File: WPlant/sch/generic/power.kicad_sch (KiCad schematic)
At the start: 47 parts, among them J2 Battery, J3 Balance, J4 DE9_Receptacle, J5 220V, U2 AP64352SP-13, U3 AP64352SP-13, U4 AP64352SP-13, U6 AP2204R-5.0

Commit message: Almost finished WP Generic
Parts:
- C10, C11, C12, C17, C18, C19, C23, C24, C25, C28, C29: footprint (none) -> Capacitor_SMD:C_0603_1608Metric_Pad1.08x0.95mm_HandSolder
- C13, C14, C15, C16, C20, C21, C22, C26, C43: footprint (none) -> Capacitor_SMD:C_1206_3216Metric_Pad1.33x1.80mm_HandSolder
- J2: footprint (none) -> local:pins4x10
- J3: footprint (none) -> Connector_JST:JST_XH_B5B-XH-A_1x05_P2.50mm_Vertical
- J4: footprint (none) -> easyeda2kicad:DB9-TH_LD09P33E4GV00LF
- R10, R11, R12, R13, R14, R15, R16, R17, R18, R20: footprint (none) -> Resistor_SMD:R_0603_1608Metric_Pad0.98x0.95mm_HandSolder
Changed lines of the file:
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@@
 			)
 		)
-		(property "Footprint" ""
+		(property "Footprint" "Capacitor_SMD:C_0603_1608Metric_Pad1.08x0.95mm_HandSolder"
 			(at 73.66 133.6548 0)
 			(effects
@@
 			)
 		)
-		(property "Footprint" ""
+		(property "Footprint" "Capacitor_SMD:C_0603_1608Metric_Pad1.08x0.95mm_HandSolder"
 			(at 86.6648 53.34 0)
 			(effects
@@
 			)
 		)
-		(property "Footprint" ""
+		(property "Footprint" "Resistor_SMD:R_0603_1608Metric_Pad0.98x0.95mm_HandSolder"
 			(at 49.022 167.64 90)
 			(effects
@@
 			)
 		)
-		(property "Footprint" ""
+		(property "Footprint" "easyeda2kicad:DB9-TH_LD09P33E4GV00LF"
 			(at 214.63 43.18 0)
 			(effects
@@
 			)
 		)
-		(property "Footprint" ""
+		(property "Footprint" "Capacitor_SMD:C_1206_3216Metric_Pad1.33x1.80mm_HandSolder"
 			(at 141.2748 104.14 0)
 			(effects
@@
 			)
 		)
-		(property "Footprint" ""
+		(property "Footprint" "Capacitor_SMD:C_0603_1608Metric_Pad1.08x0.95mm_HandSolder"
 			(at 117.1448 99.06 0)
 			(effects
@@
 			)
 		)
-		(property "Footprint" ""
+		(property "Footprint" "Capacitor_SMD:C_1206_3216Metric_Pad1.33x1.80mm_HandSolder"
 			(at 37.1348 160.02 0)
 			(effects
@@
 			)
 		)
-		(property "Footprint" ""
+		(property "Footprint" "Capacitor_SMD:C_1206_3216Metric_Pad1.33x1.80mm_HandSolder"
 			(at 128.5748 161.29 0)
 			(effects
@@
 			)
 		)
-		(property "Footprint" ""
+		(property "Footprint" "Capacitor_SMD:C_0603_1608Metric_Pad1.08x0.95mm_HandSolder"
 			(at 245.4148 143.51 0)
 			(effects
@@
 			)
 		)
-		(property "Footprint" ""
+		(property "Footprint" "local:pins4x10"
 			(at 261.62 33.02 0)
 			(effects
@@
 			)
 		)
-		(property "Footprint" ""
+		(property "Footprint" "Capacitor_SMD:C_0603_1608Metric_Pad1.08x0.95mm_HandSolder"
 			(at 86.6648 107.95 0)
 			(effects
@@
 			)
 		)
-		(property "Footprint" ""
+		(property "Footprint" "Resistor_SMD:R_0603_1608Metric_Pad0.98x0.95mm_HandSolder"
 			(at 106.172 59.69 90)
 			(effects
@@
 			)
 		)
-		(property "Footprint" ""
+		(property "Footprint" "Resistor_SMD:R_0603_1608Metric_Pad0.98x0.95mm_HandSolder"
 			(at 49.022 55.88 90)
 			(effects
@@
 			)
 		)
-		(property "Footprint" ""
+		(property "Footprint" "Capacitor_SMD:C_0603_1608Metric_Pad1.08x0.95mm_HandSolder"
 			(at 117.1448 156.21 0)
 			(effects
@@
 			)
 		)
-		(property "Footprint" ""
+		(property "Footprint" "Capacitor_SMD:C_0603_1608Metric_Pad1.08x0.95mm_HandSolder"
 			(at 73.66 21.8948 0)
 			(effects
@@
 			)
 		)
-		(property "Footprint" ""
+		(property "Footprint" "Capacitor_SMD:C_1206_3216Metric_Pad1.33x1.80mm_HandSolder"
 			(at 37.1348 102.87 0)
 			(effects
@@
 			)
 		)
-		(property "Footprint" ""
+		(property "Footprint" "Capacitor_SMD:C_0603_1608Metric_Pad1.08x0.95mm_HandSolder"
 			(at 117.1448 44.45 0)
 			(effects
@@
 			)
 		)
-		(property "Footprint" ""
+		(property "Footprint" "Capacitor_SMD:C_0603_1608Metric_Pad1.08x0.95mm_HandSolder"
 			(at 208.5848 143.51 0)
 			(effects
@@
 			)
 		)
-		(property "Footprint" ""
+		(property "Footprint" "Connector_JST:JST_XH_B5B-XH-A_1x05_P2.50mm_Vertical"
 			(at 261.62 43.18 0)
 			(effects
@@
 			)
 		)
-		(property "Footprint" ""
+		(property "Footprint" "Capacitor_SMD:C_0603_1608Metric_Pad1.08x0.95mm_HandSolder"
 			(at 86.6648 165.1 0)
 			(effects
@@
 			)
 		)
-		(property "Footprint" ""
+		(property "Footprint" "Resistor_SMD:R_0603_1608Metric_Pad0.98x0.95mm_HandSolder"
 			(at 106.172 114.3 90)
 			(effects
@@
 			)
 		)
-		(property "Footprint" ""
+		(property "Footprint" "Capacitor_SMD:C_1206_3216Metric_Pad1.33x1.80mm_HandSolder"
 			(at 141.2748 49.53 0)
 			(effects
@@
 			)
 		)
-		(property "Footprint" ""
+		(property "Footprint" "Resistor_SMD:R_0603_1608Metric_Pad0.98x0.95mm_HandSolder"
 			(at 106.172 48.26 90)
 			(effects
@@
 			)
 		)
-		(property "Footprint" ""
+		(property "Footprint" "Capacitor_SMD:C_0603_1608Metric_Pad1.08x0.95mm_HandSolder"
 			(at 73.66 76.5048 0)
 			(effects
@@
 			)
 		)
-		(property "Footprint" ""
+		(property "Footprint" "Capacitor_SMD:C_1206_3216Metric_Pad1.33x1.80mm_HandSolder"
 			(at 128.5748 104.14 0)
 			(effects
@@
 			)
 		)
-		(property "Footprint" ""
+		(property "Footprint" "Capacitor_SMD:C_1206_3216Metric_Pad1.33x1.80mm_HandSolder"
 			(at 37.1348 48.26 0)
 			(effects
@@
 			)
 		)
-		(property "Footprint" ""
+		(property "Footprint" "Resistor_SMD:R_0603_1608Metric_Pad0.98x0.95mm_HandSolder"
 			(at 106.172 102.87 90)
 			(effects
@@
 			)
 		)
-		(property "Footprint" ""
+		(property "Footprint" "Resistor_SMD:R_0603_1608Metric_Pad0.98x0.95mm_HandSolder"
 			(at 106.172 160.02 90)
 			(effects
@@
 			)
 		)
-		(property "Footprint" ""
+		(property "Footprint" "Capacitor_SMD:C_1206_3216Metric_Pad1.33x1.80mm_HandSolder"
 			(at 128.5748 49.53 0)
 			(effects
@@
 			)
 		)
-		(property "Footprint" ""
+		(property "Footprint" "Resistor_SMD:R_0603_1608Metric_Pad0.98x0.95mm_HandSolder"
 			(at 54.102 110.49 90)
 			(effects
@@
 			)
 		)
-		(property "Footprint" ""
+		(property "Footprint" "Resistor_SMD:R_0603_1608Metric_Pad0.98x0.95mm_HandSolder"
 			(at 49.022 110.49 90)
 			(effects
@@
 			)
 		)
-		(property "Footprint" ""
+		(property "Footprint" "Capacitor_SMD:C_1206_3216Metric_Pad1.33x1.80mm_HandSolder"
 			(at 141.2748 161.29 0)
 			(effects
@@
 			)
 		)
-		(property "Footprint" ""
+		(property "Footprint" "Resistor_SMD:R_0603_1608Metric_Pad0.98x0.95mm_HandSolder"
 			(at 106.172 171.45 90)
 			(effects

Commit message: Update WP Generic packages assignment
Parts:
- J2: footprint local:pins4x10 -> locals:pins4x10
- J5: footprint (none) -> easyeda2kicad:CONN-TH_HAA420A-2A
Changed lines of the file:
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@@
 			)
 		)
-		(property "Footprint" "local:pins4x10"
+		(property "Footprint" "locals:pins4x10"
 			(at 261.62 33.02 0)
 			(effects
@@
 			)
 		)
-		(property "Footprint" ""
+		(property "Footprint" "easyeda2kicad:CONN-TH_HAA420A-2A"
 			(at 205.74 93.98 0)
 			(effects

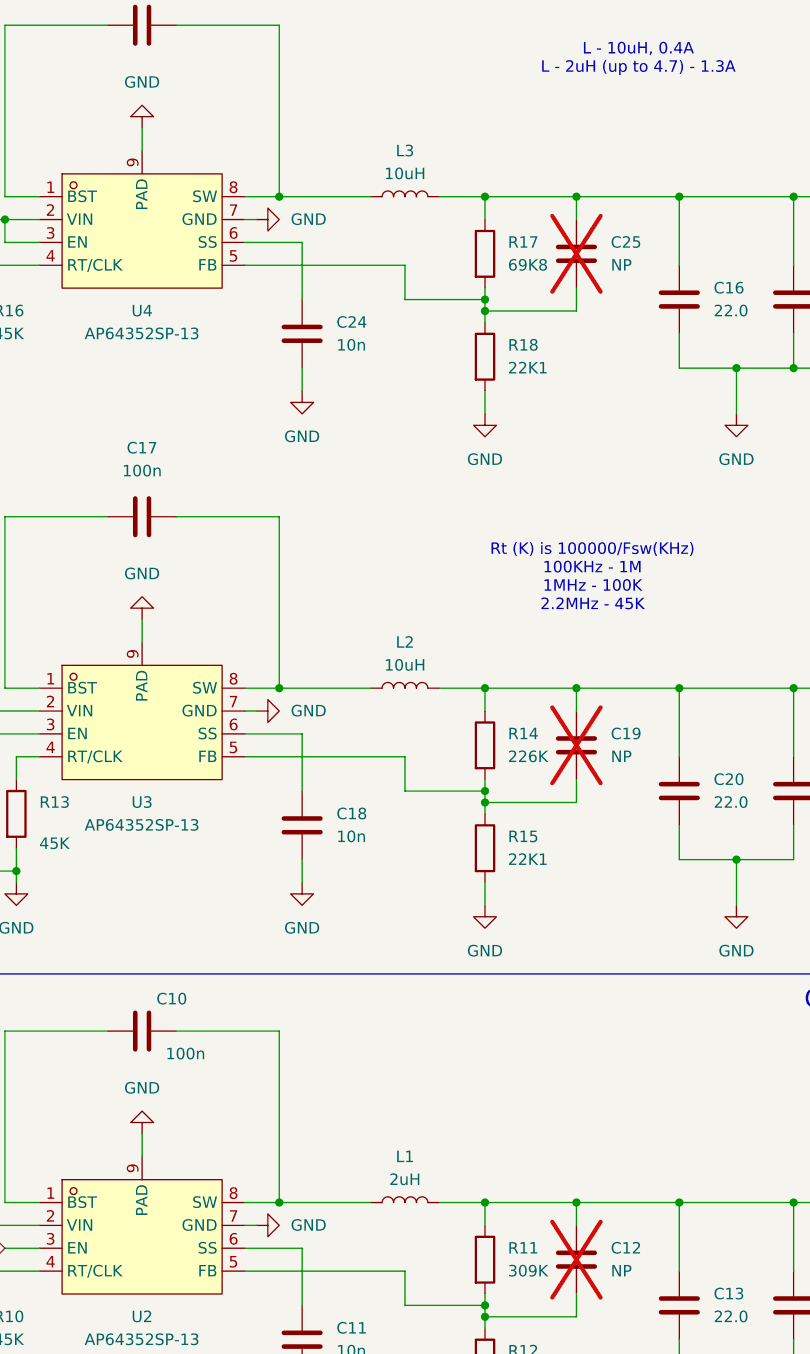
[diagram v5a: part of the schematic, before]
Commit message: Updated info for inductors for WP Generic
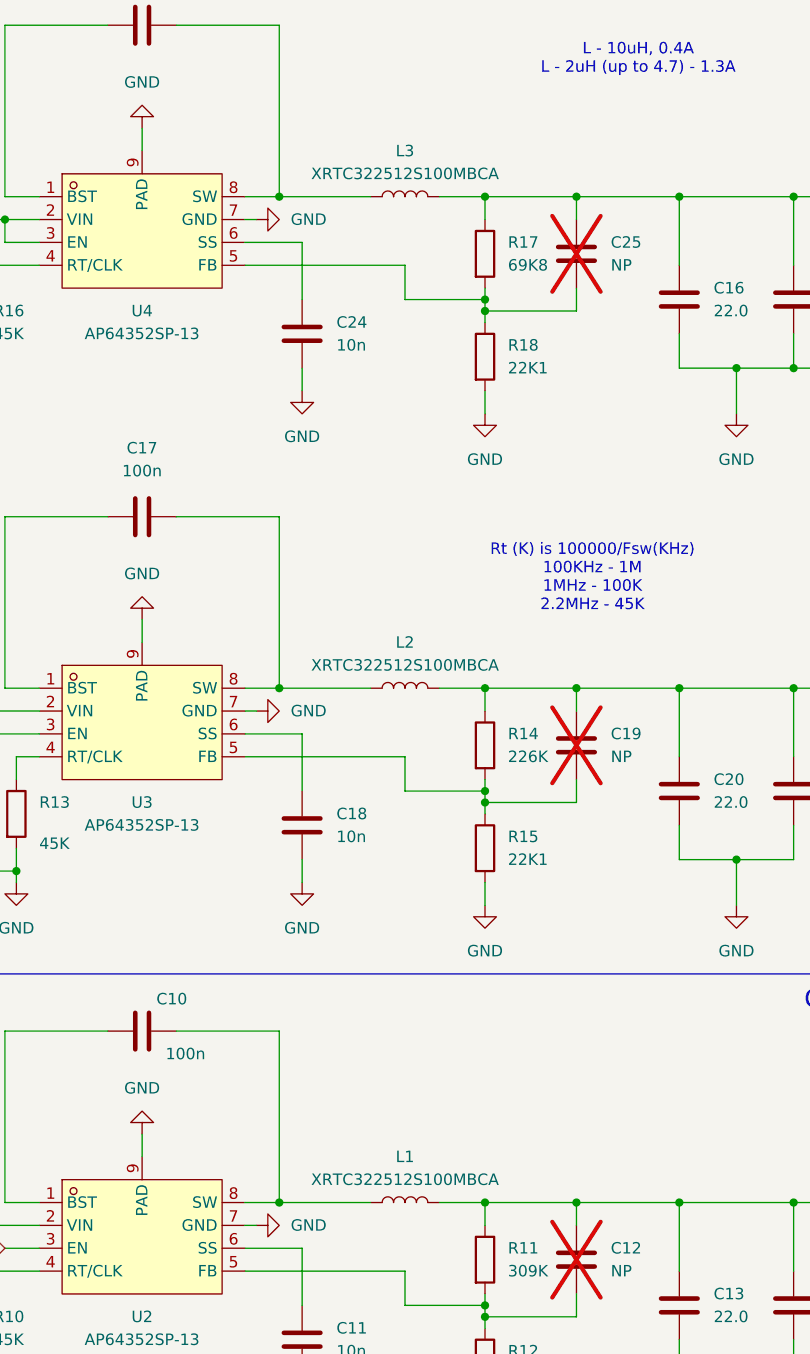
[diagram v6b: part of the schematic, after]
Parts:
- L1: value 2uH -> XRTC322512S100MBCA; footprint (none) -> locals:L_1210_XRTC; LCSC Part (none) -> C39846661
- L2, L3: value 10uH -> XRTC322512S100MBCA; footprint (none) -> locals:L_1210_XRTC; LCSC Part (none) -> C39846661
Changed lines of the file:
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@@
 			)
 		)
-		(property "Value" "10uH"
+		(property "Value" "XRTC322512S100MBCA"
 			(at 99.06 93.98 90)
 			(effects
@@
 			)
 		)
-		(property "Footprint" ""
+		(property "Footprint" "locals:L_1210_XRTC"
 			(at 99.06 96.52 0)
 			(effects
@@
 			)
 		)
+		(property "LCSC Part" "C39846661"
+			(at 99.06 96.52 0)
+			(effects
+				(font
+					(size 1.27 1.27)
+				)
+				(hide yes)
+			)
+		)
 		(pin "1"
 		)
@@
 			)
 		)
-		(property "Value" "2uH"
+		(property "Value" "XRTC322512S100MBCA"
 			(at 99.06 151.13 90)
 			(effects
@@
 			)
 		)
-		(property "Footprint" ""
+		(property "Footprint" "locals:L_1210_XRTC"
 			(at 99.06 153.67 0)
 			(effects
@@
 			)
 		)
+		(property "LCSC Part" "C39846661"
+			(at 99.06 153.67 0)
+			(effects
+				(font
+					(size 1.27 1.27)
+				)
+				(hide yes)
+			)
+		)
 		(pin "1"
 		)
@@
 			)
 		)
-		(property "Value" "10uH"
+		(property "Value" "XRTC322512S100MBCA"
 			(at 99.06 39.37 90)
 			(effects
@@
 			)
 		)
-		(property "Footprint" ""
+		(property "Footprint" "locals:L_1210_XRTC"
 			(at 99.06 41.91 0)
 			(effects
@@
 			(effects
 				(font
+					(size 1.27 1.27)
+				)
+				(hide yes)
+			)
+		)
+		(property "LCSC Part" "C39846661"
+			(at 99.06 41.91 90)
+			(effects
+				(font
